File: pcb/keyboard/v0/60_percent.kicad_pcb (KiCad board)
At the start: 2 copper layers, 180 x 90 mm, 126 parts

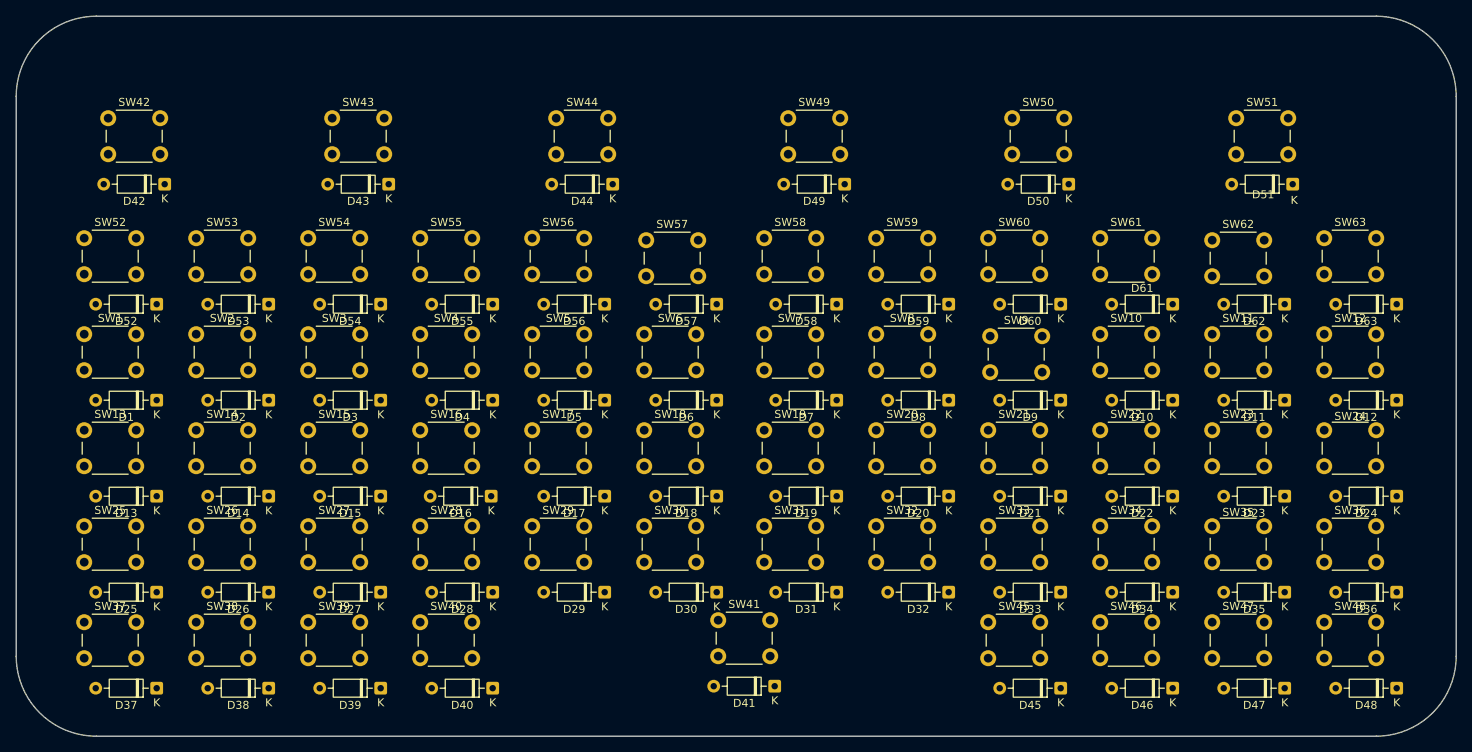
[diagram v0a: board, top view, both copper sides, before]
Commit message: Finish keyboard v0 design
This is an early version of the keyboard whose only purpose is to be a
prototype while I'm working on the firmware for it. Its not to scale, it
doesn't have an MCU, and its made entirely out of through-hole
components.
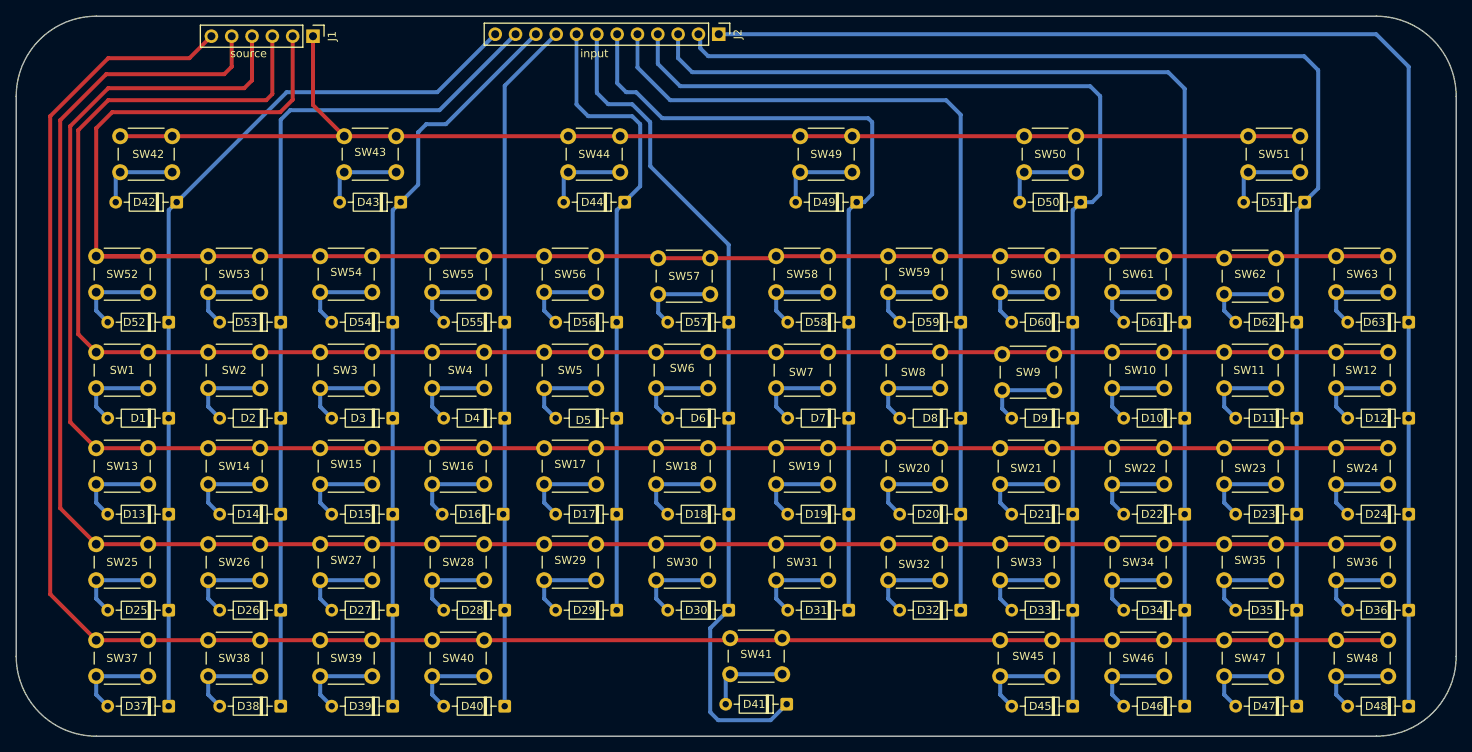
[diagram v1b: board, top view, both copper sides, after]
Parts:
- added J1: source_pins, Connector_PinHeader_2.54mm:PinHeader_1x06_P2.54mm_Vertical, F.Cu at (97.1, 52.5)
- added J2: input_pins, Connector_PinHeader_2.54mm:PinHeader_1x12_P2.54mm_Vertical, F.Cu at (147.8, 52.2)
- moved D1 2.70 mm to (79.1, 100.2)
- moved D10 2.70 mm to (206.1, 100.2)
- moved D11 2.70 mm to (220.1, 100.2)
- moved D12 2.70 mm to (234.1, 100.2)
- moved D13 2.70 mm to (79.1, 112.2)
- moved D14 2.70 mm to (93.1, 112.2)
- moved D15 2.70 mm to (107.1, 112.2)
- moved D16 2.70 mm to (120.9, 112.2)
- moved D17 2.70 mm to (135.1, 112.2)
- moved D18 2.70 mm to (149.1, 112.2)
- moved D19 2.70 mm to (164.1, 112.2)
- moved D2 2.70 mm to (93.1, 100.2)
- moved D20 2.70 mm to (178.1, 112.2)
- moved D21 2.70 mm to (192.1, 112.2)
- moved D22 2.70 mm to (206.1, 112.2)
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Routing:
- net Net-(J1-Pin_6): track 0.00 -> 253.7 mm
- net Net-(J1-Pin_5): track 0.00 -> 244.4 mm
- net Net-(J1-Pin_4): track 0.00 -> 233.7 mm
- net Net-(J1-Pin_2): track 0.00 -> 232.2 mm
- net Net-(J1-Pin_3): track 0.00 -> 223.6 mm
- net Net-(D12-K): track 0.00 -> 167.9 mm
- net Net-(J1-Pin_1): track 0.00 -> 161.6 mm
- net Net-(D11-K): track 0.00 -> 160.8 mm
- net Net-(D10-K): track 0.00 -> 145.1 mm
- net Net-(D21-K): track 0.00 -> 139.2 mm
- net Net-(D1-K): track 0.00 -> 111.9 mm
- net Net-(D20-K): track 0.00 -> 108.9 mm
- net Net-(D14-K): track 0.00 -> 107.1 mm
- net Net-(D18-K): track 0.00 -> 105.1 mm
- net Net-(D19-K): track 0.00 -> 102.8 mm
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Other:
- board text added: "input"
- board text added: "source"
